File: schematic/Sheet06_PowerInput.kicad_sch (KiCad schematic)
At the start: 9 parts, among them J1 POWER_IN, U10 INA214-SP

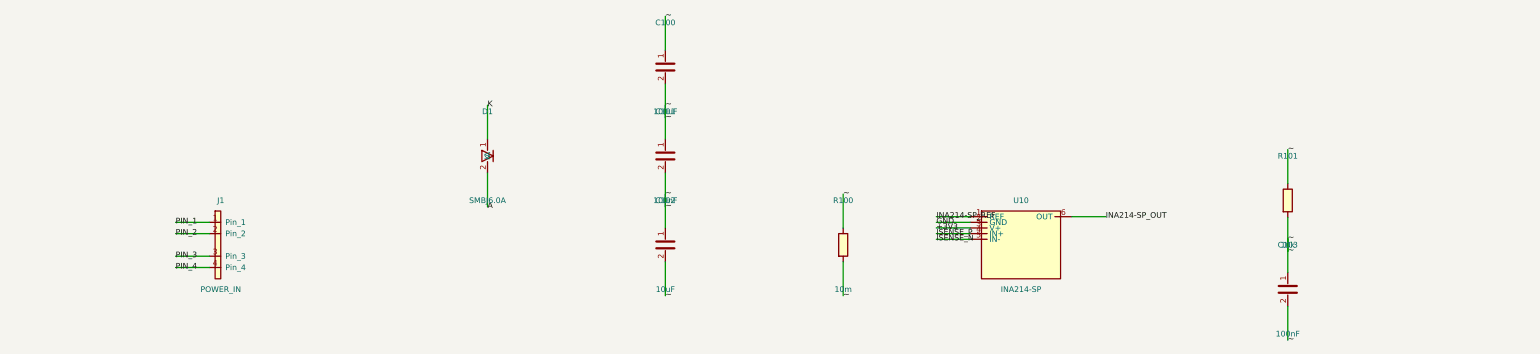
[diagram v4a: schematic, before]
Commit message: fix: use horizontal wire stubs to prevent KiCad net merging
Root cause: vertical wires from stacked power pins (1.27mm spacing)
overlapped when wire length > pin spacing, causing KiCad to merge
all power nets into one. Also skip unnamed (~) passive component pins.

Changes:
- Always use horizontal LEFT stubs regardless of pin angle
- Skip pins with net_name '~' (capacitor/resistor unnamed pins)
- 557 pin connections across 13 sheets, all pass KiCad CLI

NOTE: power net separation still shows all power_in pins on one net
in kicad-cli netlist export - needs further investigation.
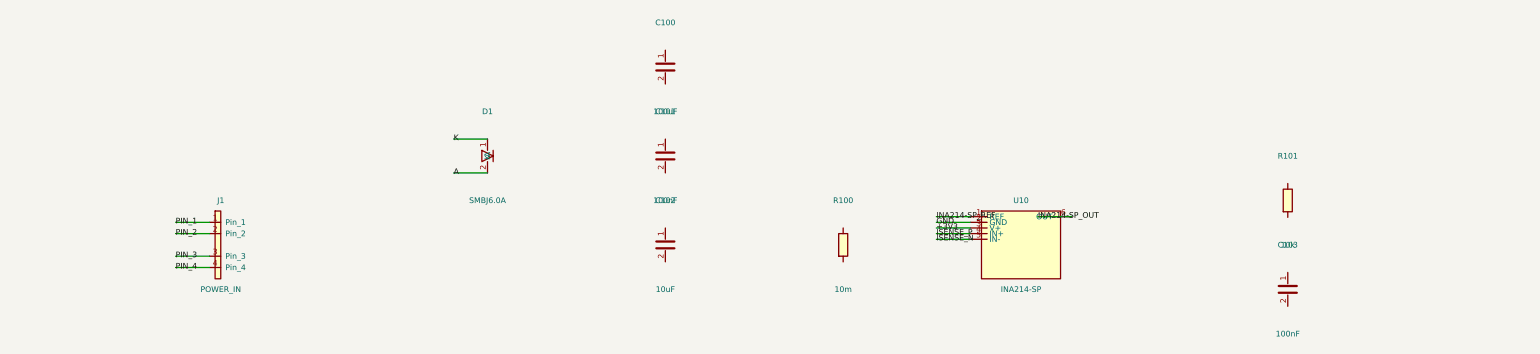
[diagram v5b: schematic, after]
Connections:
- removed net ~: C100.1, C100.2, C101.1, C101.2, C102.1, C102.2, C103.1, C103.2, R100.1, R100.2, R101.1, R101.2
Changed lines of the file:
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@@
   (wire (pts (xy 57.4600 85.0800) (xy 49.8400 85.0800)) (stroke (width 0) (type default)))
   (label "PIN_4" (at 49.8400 85.0800 0) (effects (font (size 1.27 1.27))))
-  (wire (pts (xy 120.0000 56.1900) (xy 120.0000 48.5700)) (stroke (width 0) (type default)))
-  (label "K" (at 120.0000 48.5700 0) (effects (font (size 1.27 1.27))))
-  (wire (pts (xy 120.0000 63.8100) (xy 120.0000 71.4300)) (stroke (width 0) (type default)))
-  (label "A" (at 120.0000 71.4300 0) (effects (font (size 1.27 1.27))))
-  (wire (pts (xy 160.0000 36.1900) (xy 160.0000 28.5700)) (stroke (width 0) (type default)))
-  (label "~" (at 160.0000 28.5700 0) (effects (font (size 1.27 1.27))))
-  (wire (pts (xy 160.0000 43.8100) (xy 160.0000 51.4300)) (stroke (width 0) (type default)))
-  (label "~" (at 160.0000 51.4300 0) (effects (font (size 1.27 1.27))))
-  (wire (pts (xy 160.0000 56.1900) (xy 160.0000 48.5700)) (stroke (width 0) (type default)))
-  (label "~" (at 160.0000 48.5700 0) (effects (font (size 1.27 1.27))))
-  (wire (pts (xy 160.0000 63.8100) (xy 160.0000 71.4300)) (stroke (width 0) (type default)))
-  (label "~" (at 160.0000 71.4300 0) (effects (font (size 1.27 1.27))))
-  (wire (pts (xy 160.0000 76.1900) (xy 160.0000 68.5700)) (stroke (width 0) (type default)))
-  (label "~" (at 160.0000 68.5700 0) (effects (font (size 1.27 1.27))))
-  (wire (pts (xy 160.0000 83.8100) (xy 160.0000 91.4300)) (stroke (width 0) (type default)))
-  (label "~" (at 160.0000 91.4300 0) (effects (font (size 1.27 1.27))))
+  (wire (pts (xy 120.0000 56.1900) (xy 112.3800 56.1900)) (stroke (width 0) (type default)))
+  (label "K" (at 112.3800 56.1900 0) (effects (font (size 1.27 1.27))))
+  (wire (pts (xy 120.0000 63.8100) (xy 112.3800 63.8100)) (stroke (width 0) (type default)))
+  (label "A" (at 112.3800 63.8100 0) (effects (font (size 1.27 1.27))))
   (wire (pts (xy 228.5700 73.6500) (xy 220.9500 73.6500)) (stroke (width 0) (type default)))
   (label "INA214-SP_REF" (at 220.9500 73.6500 0) (effects (font (size 1.27 1.27))))
@@
   (wire (pts (xy 228.5700 78.7300) (xy 220.9500 78.7300)) (stroke (width 0) (type default)))
   (label "ISENSE_N" (at 220.9500 78.7300 0) (effects (font (size 1.27 1.27))))
-  (wire (pts (xy 251.4300 73.6500) (xy 259.0500 73.6500)) (stroke (width 0) (type default)))
-  (label "INA214-SP_OUT" (at 259.0500 73.6500 0) (effects (font (size 1.27 1.27))))
-  (wire (pts (xy 200.0000 76.1900) (xy 200.0000 68.5700)) (stroke (width 0) (type default)))
-  (label "~" (at 200.0000 68.5700 0) (effects (font (size 1.27 1.27))))
-  (wire (pts (xy 200.0000 83.8100) (xy 200.0000 91.4300)) (stroke (width 0) (type default)))
-  (label "~" (at 200.0000 91.4300 0) (effects (font (size 1.27 1.27))))
-  (wire (pts (xy 300.0000 66.1900) (xy 300.0000 58.5700)) (stroke (width 0) (type default)))
-  (label "~" (at 300.0000 58.5700 0) (effects (font (size 1.27 1.27))))
-  (wire (pts (xy 300.0000 73.8100) (xy 300.0000 81.4300)) (stroke (width 0) (type default)))
-  (label "~" (at 300.0000 81.4300 0) (effects (font (size 1.27 1.27))))
-  (wire (pts (xy 300.0000 86.1900) (xy 300.0000 78.5700)) (stroke (width 0) (type default)))
-  (label "~" (at 300.0000 78.5700 0) (effects (font (size 1.27 1.27))))
-  (wire (pts (xy 300.0000 93.8100) (xy 300.0000 101.4300)) (stroke (width 0) (type default)))
-  (label "~" (at 300.0000 101.4300 0) (effects (font (size 1.27 1.27))))
+  (wire (pts (xy 251.4300 73.6500) (xy 243.8100 73.6500)) (stroke (width 0) (type default)))
+  (label "INA214-SP_OUT" (at 243.8100 73.6500 0) (effects (font (size 1.27 1.27))))
   (sheet_instances (path "/" (page "1")))
 )

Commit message: fix: replace wire stubs with labels-only to prevent power net shorts
Labels placed directly at pin endpoints eliminate wire overlap that
caused BGA power pins (VA11, VA19, VD11, AGND, DGND) to merge into
a single net. Verified via netlist: GND=52, +1V0_ANA=12, +1V9_ANA=12,
+1V1_DIG=10 nodes (all correct per datasheet pin mapping).
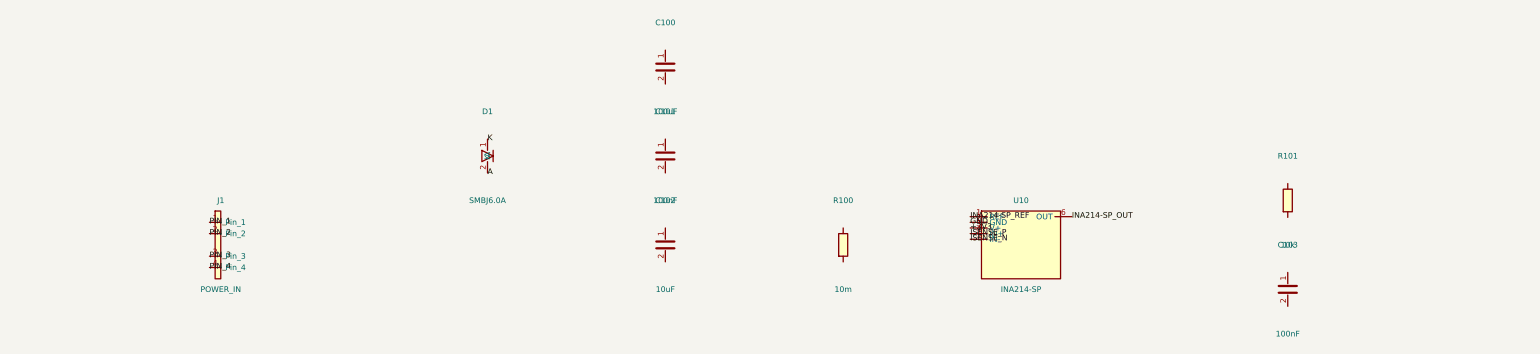
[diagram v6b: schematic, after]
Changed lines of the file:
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@@
     (pin "2")
   )
-  (wire (pts (xy 57.4600 74.9200) (xy 49.8400 74.9200)) (stroke (width 0) (type default)))
-  (label "PIN_1" (at 49.8400 74.9200 0) (effects (font (size 1.27 1.27))))
-  (wire (pts (xy 57.4600 77.4600) (xy 49.8400 77.4600)) (stroke (width 0) (type default)))
-  (label "PIN_2" (at 49.8400 77.4600 0) (effects (font (size 1.27 1.27))))
-  (wire (pts (xy 57.4600 82.5400) (xy 49.8400 82.5400)) (stroke (width 0) (type default)))
-  (label "PIN_3" (at 49.8400 82.5400 0) (effects (font (size 1.27 1.27))))
-  (wire (pts (xy 57.4600 85.0800) (xy 49.8400 85.0800)) (stroke (width 0) (type default)))
-  (label "PIN_4" (at 49.8400 85.0800 0) (effects (font (size 1.27 1.27))))
-  (wire (pts (xy 120.0000 56.1900) (xy 112.3800 56.1900)) (stroke (width 0) (type default)))
-  (label "K" (at 112.3800 56.1900 0) (effects (font (size 1.27 1.27))))
-  (wire (pts (xy 120.0000 63.8100) (xy 112.3800 63.8100)) (stroke (width 0) (type default)))
-  (label "A" (at 112.3800 63.8100 0) (effects (font (size 1.27 1.27))))
-  (wire (pts (xy 228.5700 73.6500) (xy 220.9500 73.6500)) (stroke (width 0) (type default)))
-  (label "INA214-SP_REF" (at 220.9500 73.6500 0) (effects (font (size 1.27 1.27))))
-  (wire (pts (xy 228.5700 74.9200) (xy 220.9500 74.9200)) (stroke (width 0) (type default)))
-  (label "GND" (at 220.9500 74.9200 0) (effects (font (size 1.27 1.27))))
-  (wire (pts (xy 228.5700 76.1900) (xy 220.9500 76.1900)) (stroke (width 0) (type default)))
-  (label "+3V3" (at 220.9500 76.1900 0) (effects (font (size 1.27 1.27))))
-  (wire (pts (xy 228.5700 77.4600) (xy 220.9500 77.4600)) (stroke (width 0) (type default)))
-  (label "ISENSE_P" (at 220.9500 77.4600 0) (effects (font (size 1.27 1.27))))
-  (wire (pts (xy 228.5700 78.7300) (xy 220.9500 78.7300)) (stroke (width 0) (type default)))
-  (label "ISENSE_N" (at 220.9500 78.7300 0) (effects (font (size 1.27 1.27))))
-  (wire (pts (xy 251.4300 73.6500) (xy 243.8100 73.6500)) (stroke (width 0) (type default)))
-  (label "INA214-SP_OUT" (at 243.8100 73.6500 0) (effects (font (size 1.27 1.27))))
+  (label "PIN_1" (at 57.4600 74.9200 0) (effects (font (size 1.27 1.27))))
+  (label "PIN_2" (at 57.4600 77.4600 0) (effects (font (size 1.27 1.27))))
+  (label "PIN_3" (at 57.4600 82.5400 0) (effects (font (size 1.27 1.27))))
+  (label "PIN_4" (at 57.4600 85.0800 0) (effects (font (size 1.27 1.27))))
+  (label "K" (at 120.0000 56.1900 0) (effects (font (size 1.27 1.27))))
+  (label "A" (at 120.0000 63.8100 0) (effects (font (size 1.27 1.27))))
+  (label "INA214-SP_REF" (at 228.5700 73.6500 0) (effects (font (size 1.27 1.27))))
+  (label "GND" (at 228.5700 74.9200 0) (effects (font (size 1.27 1.27))))
+  (label "+3V3" (at 228.5700 76.1900 0) (effects (font (size 1.27 1.27))))
+  (label "ISENSE_P" (at 228.5700 77.4600 0) (effects (font (size 1.27 1.27))))
+  (label "ISENSE_N" (at 228.5700 78.7300 0) (effects (font (size 1.27 1.27))))
+  (label "INA214-SP_OUT" (at 251.4300 73.6500 0) (effects (font (size 1.27 1.27))))
   (sheet_instances (path "/" (page "1")))
 )

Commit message: fix: isolate ISL70003ASEH buck pins, fix LMX_SYNC collision, NC pins, connector pin names
- ISL70003ASEH pins now use ref prefix (U6_LX1 vs U7_LX1) to prevent shorts
- Buck SYNC pins separated from LMX_SYNC (power sync ≠ PLL sync)
- NC pins properly skipped (unconnected)
- Connector PIN_1..PIN_6 use ref prefix (J1_PIN_1 vs J2_PIN_1)
- Fixed annotation warnings in Sheet13 (C_dev→C125, R_dev→R74, U_TPS7H→U14)
- Regenerated all PDFs and SVGs
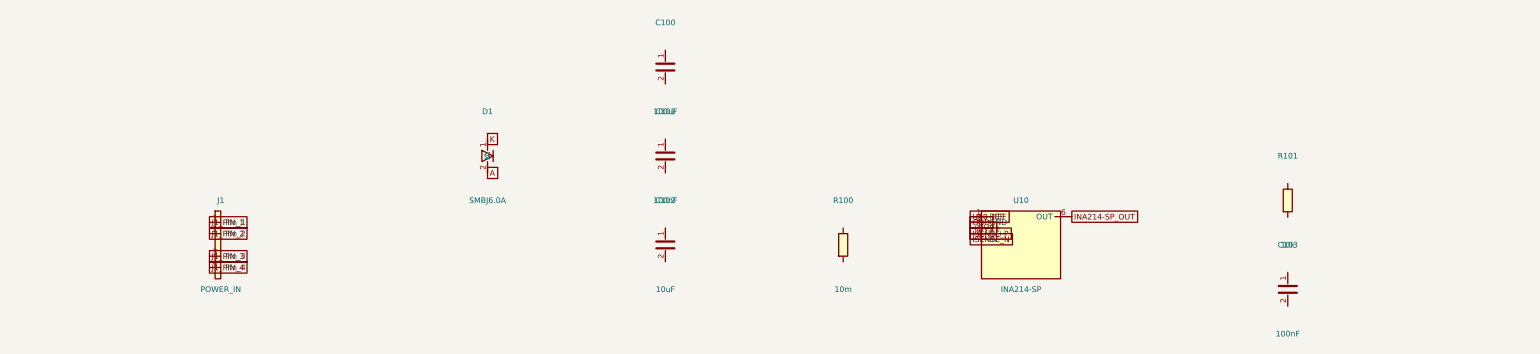
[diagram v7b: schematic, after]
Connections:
- net INA214-SP_REF renamed U10_REF
- net PIN_1 renamed J1_PIN_1
- net PIN_2 renamed J1_PIN_2
- net PIN_3 renamed J1_PIN_3
- net PIN_4 renamed J1_PIN_4
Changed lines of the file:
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@@
     (pin "2")
   )
-  (label "PIN_1" (at 57.4600 74.9200 0) (effects (font (size 1.27 1.27))))
-  (label "PIN_2" (at 57.4600 77.4600 0) (effects (font (size 1.27 1.27))))
-  (label "PIN_3" (at 57.4600 82.5400 0) (effects (font (size 1.27 1.27))))
-  (label "PIN_4" (at 57.4600 85.0800 0) (effects (font (size 1.27 1.27))))
-  (label "K" (at 120.0000 56.1900 0) (effects (font (size 1.27 1.27))))
-  (label "A" (at 120.0000 63.8100 0) (effects (font (size 1.27 1.27))))
-  (label "INA214-SP_REF" (at 228.5700 73.6500 0) (effects (font (size 1.27 1.27))))
-  (label "GND" (at 228.5700 74.9200 0) (effects (font (size 1.27 1.27))))
-  (label "+3V3" (at 228.5700 76.1900 0) (effects (font (size 1.27 1.27))))
-  (label "ISENSE_P" (at 228.5700 77.4600 0) (effects (font (size 1.27 1.27))))
-  (label "ISENSE_N" (at 228.5700 78.7300 0) (effects (font (size 1.27 1.27))))
-  (label "INA214-SP_OUT" (at 251.4300 73.6500 0) (effects (font (size 1.27 1.27))))
+  (global_label "J1_PIN_1" (at 57.4600 74.9200 0) (effects (font (size 1.27 1.27))))
+  (global_label "J1_PIN_2" (at 57.4600 77.4600 0) (effects (font (size 1.27 1.27))))
+  (global_label "J1_PIN_3" (at 57.4600 82.5400 0) (effects (font (size 1.27 1.27))))
+  (global_label "J1_PIN_4" (at 57.4600 85.0800 0) (effects (font (size 1.27 1.27))))
+  (global_label "K" (at 120.0000 56.1900 0) (effects (font (size 1.27 1.27))))
+  (global_label "A" (at 120.0000 63.8100 0) (effects (font (size 1.27 1.27))))
+  (global_label "U10_REF" (at 228.5700 73.6500 0) (effects (font (size 1.27 1.27))))
+  (global_label "GND" (at 228.5700 74.9200 0) (effects (font (size 1.27 1.27))))
+  (global_label "+3V3" (at 228.5700 76.1900 0) (effects (font (size 1.27 1.27))))
+  (global_label "ISENSE_P" (at 228.5700 77.4600 0) (effects (font (size 1.27 1.27))))
+  (global_label "ISENSE_N" (at 228.5700 78.7300 0) (effects (font (size 1.27 1.27))))
+  (global_label "INA214-SP_OUT" (at 251.4300 73.6500 0) (effects (font (size 1.27 1.27))))
   (sheet_instances (path "/" (page "1")))
 )

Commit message: feat: connect ALL passive components and fix clock routing
- Added PASSIVE_TOPOLOGY dict mapping 139 passives to their nets
- Passive pin endpoints now get global_labels (was 0 connected, now 138)
- R38 intentionally GND-GND (RECAL_EN pull-down)
- Fixed LMK clock output mapping: CLKout0→ADC_CLK_P, CLKout2→FPGA_REFCLK_P, etc.
- Fixed TPS7H5001-SP SYNC pin collision with LMX_SYNC
- Total connections: 867 pins (up from 641)
- Cross-sheet nets: 52
- Power rails: VIN(33), +3V3(98), GND(228) all with decoupling
- JESD204C: U1↔U2 on 4 lanes ✓
- SPI: U1↔U2↔U3↔U4 ✓
- Clock: LMK→ADC (CLK+SYSREF), LMK→FPGA (REF+SPW) ✓
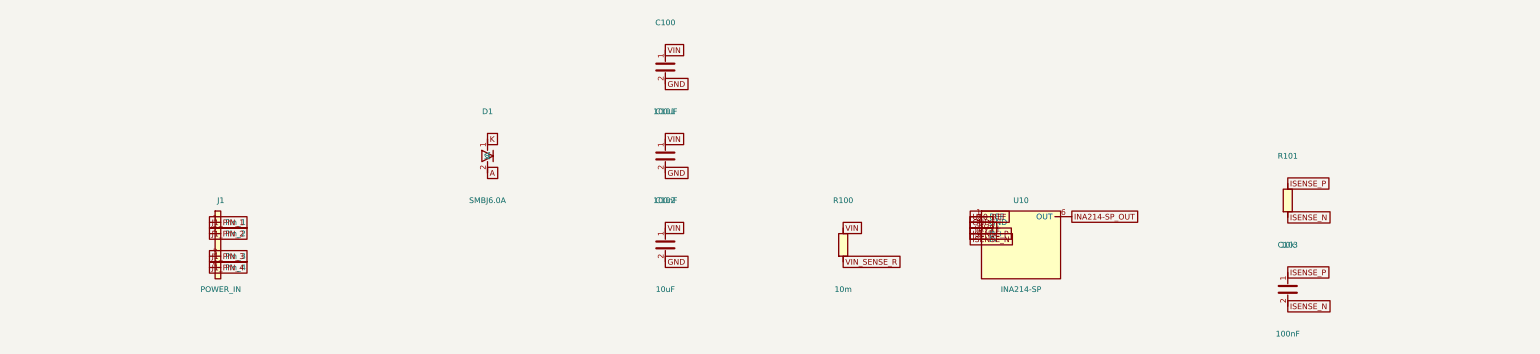
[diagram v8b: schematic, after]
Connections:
- net GND: now also C100.2, C101.2, C102.2
- net ISENSE_N: now also C103.2, R101.2
- net ISENSE_P: now also C103.1, R101.1
- net VIN: now reaches C102.1
- net VIN: now also C100.1, C101.1, R100.1
- net VIN_SENSE_R: now reaches R100.2
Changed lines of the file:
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@@
   (global_label "ISENSE_N" (at 228.5700 78.7300 0) (effects (font (size 1.27 1.27))))
   (global_label "INA214-SP_OUT" (at 251.4300 73.6500 0) (effects (font (size 1.27 1.27))))
+  (global_label "VIN" (at 160.0000 36.1900 0) (effects (font (size 1.27 1.27))))
+  (global_label "GND" (at 160.0000 43.8100 0) (effects (font (size 1.27 1.27))))
+  (global_label "VIN" (at 160.0000 56.1900 0) (effects (font (size 1.27 1.27))))
+  (global_label "GND" (at 160.0000 63.8100 0) (effects (font (size 1.27 1.27))))
+  (global_label "VIN" (at 160.0000 76.1900 0) (effects (font (size 1.27 1.27))))
+  (global_label "GND" (at 160.0000 83.8100 0) (effects (font (size 1.27 1.27))))
+  (global_label "VIN" (at 200.0000 76.1900 0) (effects (font (size 1.27 1.27))))
+  (global_label "VIN_SENSE_R" (at 200.0000 83.8100 0) (effects (font (size 1.27 1.27))))
+  (global_label "ISENSE_P" (at 300.0000 66.1900 0) (effects (font (size 1.27 1.27))))
+  (global_label "ISENSE_N" (at 300.0000 73.8100 0) (effects (font (size 1.27 1.27))))
+  (global_label "ISENSE_P" (at 300.0000 86.1900 0) (effects (font (size 1.27 1.27))))
+  (global_label "ISENSE_N" (at 300.0000 93.8100 0) (effects (font (size 1.27 1.27))))
   (sheet_instances (path "/" (page "1")))
 )
